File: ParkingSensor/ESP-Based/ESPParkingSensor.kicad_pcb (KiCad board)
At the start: 2 copper layers, 10 parts, among them P1 CONN_UART, P2 CONN_WS2812, P3 CONN_01X02, P4 CONN_US, U1 ESP-12E, U2 AP1117

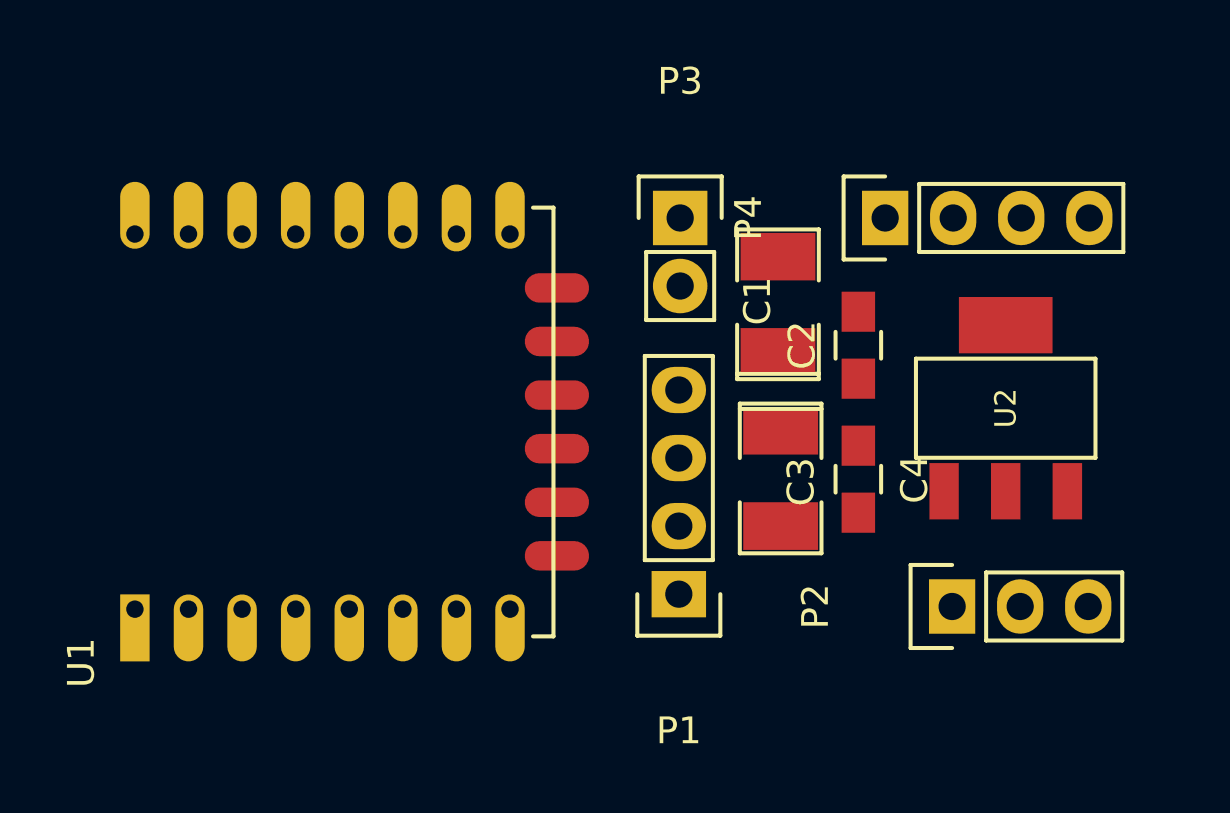
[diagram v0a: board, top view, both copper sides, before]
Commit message: changed the braces to be in the right place on loop() and setup()
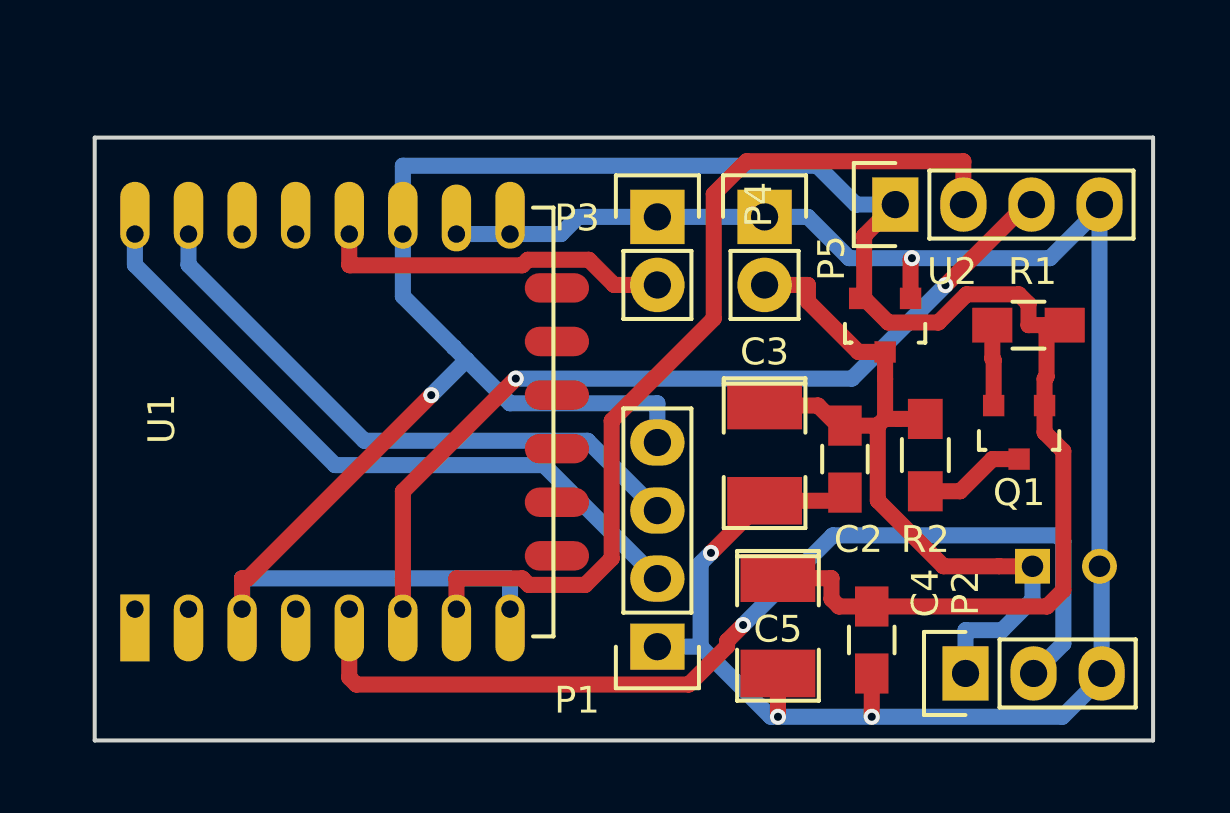
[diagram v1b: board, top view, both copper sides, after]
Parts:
- added C5: 2.2uf, SMD_Packages:SMD-1210_Pol, F.Cu at (163.0, 109.2)
- added P5: CONN_01X02, Pin_Headers:Pin_Header_Straight_1x02, F.Cu at (162.5, 94.0)
- added Q1: BSS138, TO_SOT_Packages_SMD:SOT-23, F.Cu at (172.0, 102.0)
- added R1: 10k, Resistors_SMD:R_0805_HandSoldering, F.Cu at (172.3, 98.0)
- added R2: 10k, Resistors_SMD:R_0805_HandSoldering, F.Cu at (168.5, 102.8)
- C1: value CP -> 1000uf; footprint SMD_Packages:SMD-1210_Pol -> Capacitors_ThroughHole:C_Radial_D6.3_L11.2_P2.5; moved to B.Cu
- C2, C4: value C -> 0.1uf
- C3: value CP -> 2.2uf
- U2: value AP1117 -> MCP1700; footprint so23-8:SOT-223 -> TO_SOT_Packages_SMD:SOT-23
- moved C1 13.6 mm to (172.5, 107.0), turned to 0 degrees
- moved C4 6.02 mm to (166.5, 109.8)
- moved U2 5.46 mm to (167.0, 98.0), turned to 180 degrees
- moved C2 4.28 mm to (165.5, 103.0), turned to 270 degrees
- moved P2 2.55 mm to (170.0, 111.0)
- moved P1 2.12 mm to (158.5, 110.0)
- moved C3 1.12 mm to (162.5, 102.8)
- moved P3 0.85 mm to (158.5, 94.0)
- moved P4 0.63 mm to (167.4, 93.5)
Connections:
- C3 pad 1: +3V3 -> +5V
- P2 pad 1: +3V3 -> +5V
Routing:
- net +3V3: track 0.00 -> 97.1 mm, vias 0 -> 1
- net GND: track 0.00 -> 76.1 mm, vias 0 -> 4
- net BB_LINE: track 0.00 -> 37.2 mm, vias 0 -> 1
- net TRG: track 0.00 -> 34.1 mm
- net ECHO: track 0.00 -> 32.3 mm, vias 0 -> 2
- net +5V: track 0.00 -> 30.2 mm
- net Net-(P1-Pad2): track 0.00 -> 25.5 mm
- net Net-(P1-Pad3): track 0.00 -> 22.4 mm
- net PRG: track 0.00 -> 13.1 mm
- net GPIO2_5: track 0.00 -> 4.00 mm
- net GPIO2: track 0.00 -> 3.02 mm
- added copper zone on F.Cu, net +3V3
- added copper zone on B.Cu, net GND
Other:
- board outline added: 39.5 x 22.5 mm
- net class Default: trace_width 0.4 -> 0.6
- board text added: "Takigama https://github.com/takigama Parking Sensor me@pjr.cc"

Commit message: forgot to route thru the level converter
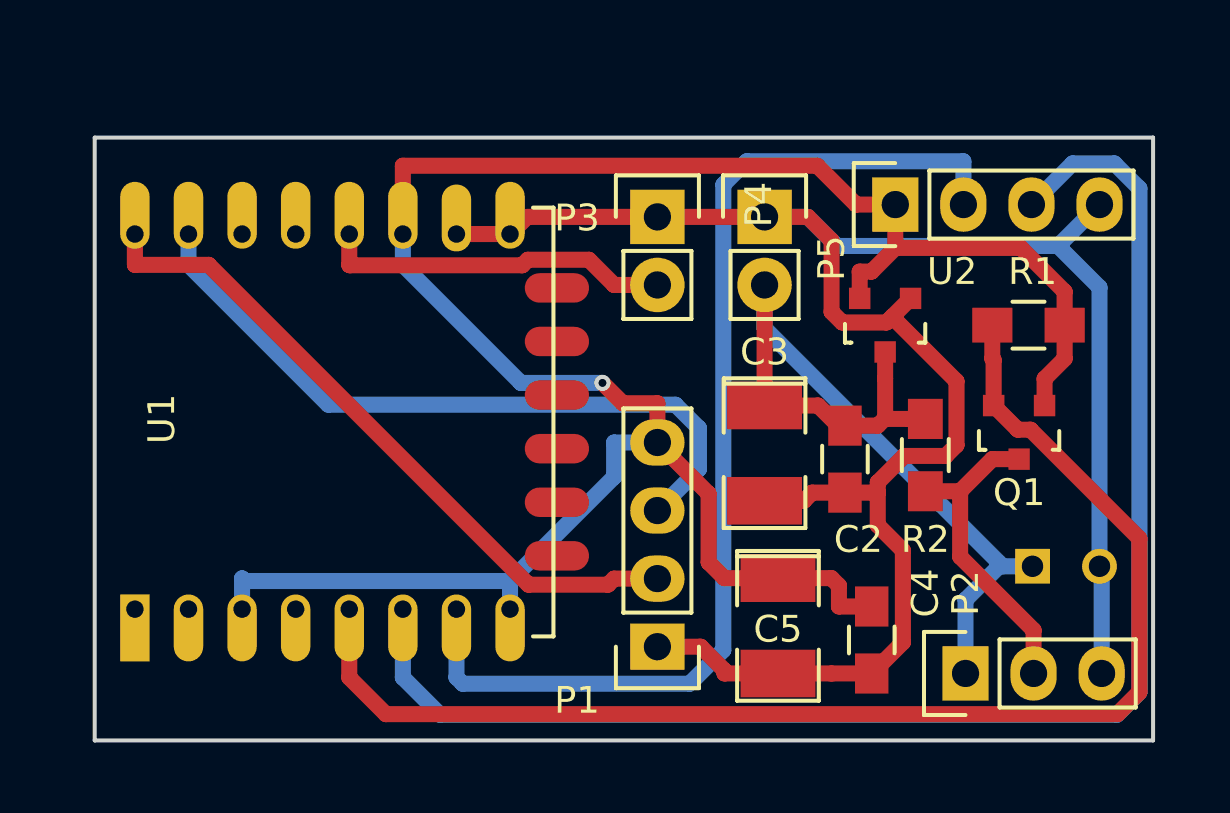
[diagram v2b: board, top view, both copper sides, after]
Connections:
- P2 pad 2: BB_LINE -> BB_LINE_5
- Q1 pad 2: GPIO2 -> BB_LINE
- Q1 pad 3: GPIO2_5 -> BB_LINE_5
- R1 pad 2: GPIO2 -> BB_LINE
- R2 pad 2: GPIO2_5 -> BB_LINE_5
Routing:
- net ECHO: track 32.3 -> 54.8 mm, vias 2 -> 0
- net +3V3: track 97.1 -> 84.8 mm
- net BB_LINE: track 37.2 -> 49.2 mm, vias 1 -> 0
- net BB_LINE_5: track 0.00 -> 11.9 mm
- net TRG: track 34.1 -> 41.4 mm
- net GND: track 76.1 -> 81.1 mm, vias 4 -> 0
- net GPIO2_5: track 4.00 -> 0.00 mm
- net Net-(P1-Pad3): track 22.4 -> 26.4 mm
- net +5V: track 30.2 -> 33.3 mm
- net GPIO2: track 3.02 -> 0.00 mm
- removed copper zone on F.Cu, net +3V3
- removed copper zone on B.Cu, net GND

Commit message: moved to 5v hc-sr04 simplified
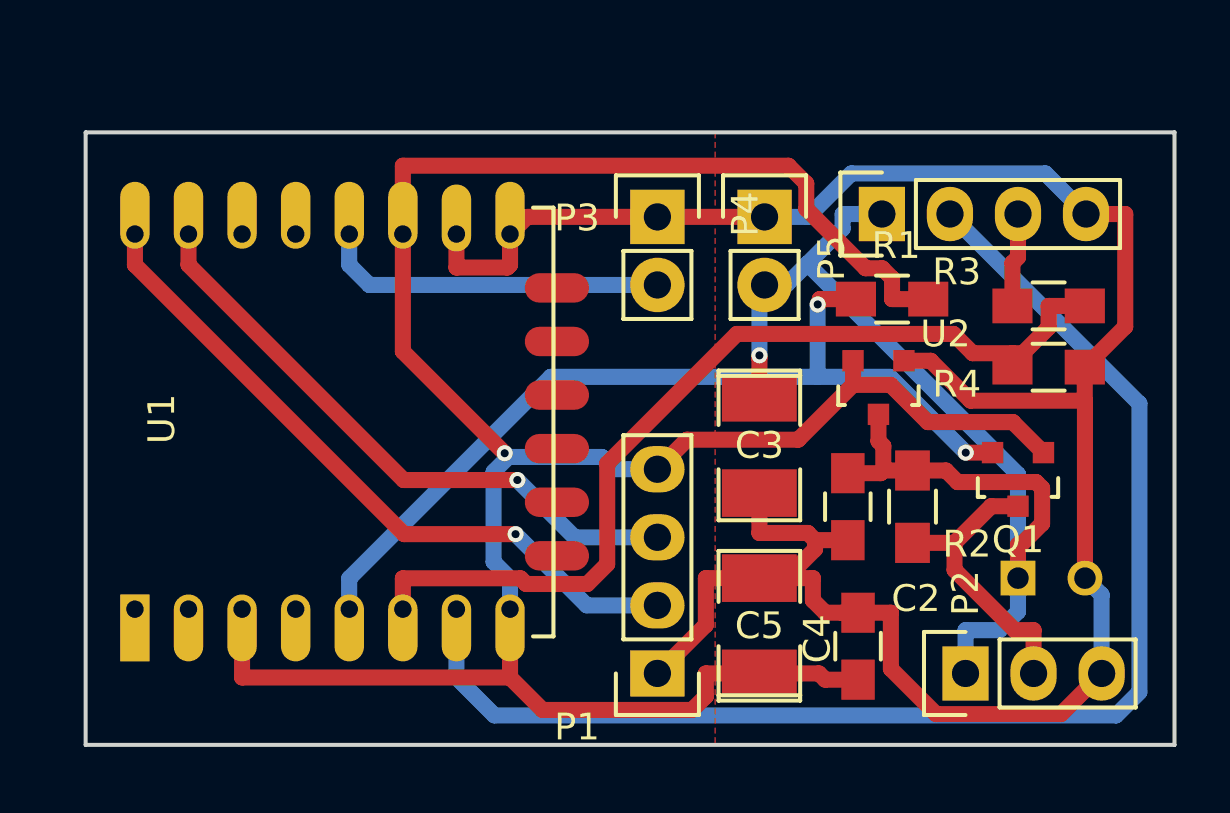
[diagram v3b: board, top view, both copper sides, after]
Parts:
- added R3: 1.7k, Resistors_SMD:R_0805_HandSoldering, F.Cu at (173.1, 97.3)
- added R4: 3.3k, Resistors_SMD:R_0805_HandSoldering, F.Cu at (173.1, 99.6)
- moved R1 5.18 mm to (167.3, 97.0)
- moved U2 2.34 mm to (166.8, 100.3)
- moved R2 1.98 mm to (168.0, 104.8)
- moved C2 1.78 mm to (165.6, 104.8)
- moved Q1 1.76 mm to (172.0, 103.8)
- moved P1 1.00 mm to (158.5, 111.0)
- moved C1 0.70 mm to (172.0, 107.4)
- moved C5 0.69 mm to (162.3, 109.2), turned to 90 degrees
- moved P4 0.61 mm to (166.9, 93.9)
- moved C4 0.56 mm to (166.0, 110.0), turned to 90 degrees
- moved C3 0.35 mm to (162.3, 102.5)
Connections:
- P4 pad 1: +3V3 -> +5V
- U1 pad 6: ECHO -> Net-(R3-Pad2)
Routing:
- net ECHO: track 54.8 -> 3.51 mm
- net Net-(R3-Pad2): track 0.00 -> 34.8 mm
- net BB_LINE: track 49.2 -> 33.7 mm, vias 0 -> 2
- net +5V: track 33.3 -> 43.9 mm, vias 0 -> 1
- net +3V3: track 84.8 -> 94.5 mm
- net TRG: track 41.4 -> 49.8 mm
- net Net-(P1-Pad3): track 26.4 -> 22.9 mm, vias 0 -> 1
- net GND: track 81.1 -> 84.7 mm
- net BB_LINE_5: track 11.9 -> 11.0 mm
- net Net-(P1-Pad2): track 25.7 -> 25.9 mm, vias 0 -> 1
- added copper zone on F.Cu, net +5V
- added copper zone on B.Cu, net GND
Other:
- board size 39.5 x 22.5 mm -> 40.6 x 22.9 mm
